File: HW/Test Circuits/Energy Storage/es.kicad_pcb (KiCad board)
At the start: 2 copper layers, 5 parts, among them J1 IN, J2 OUT

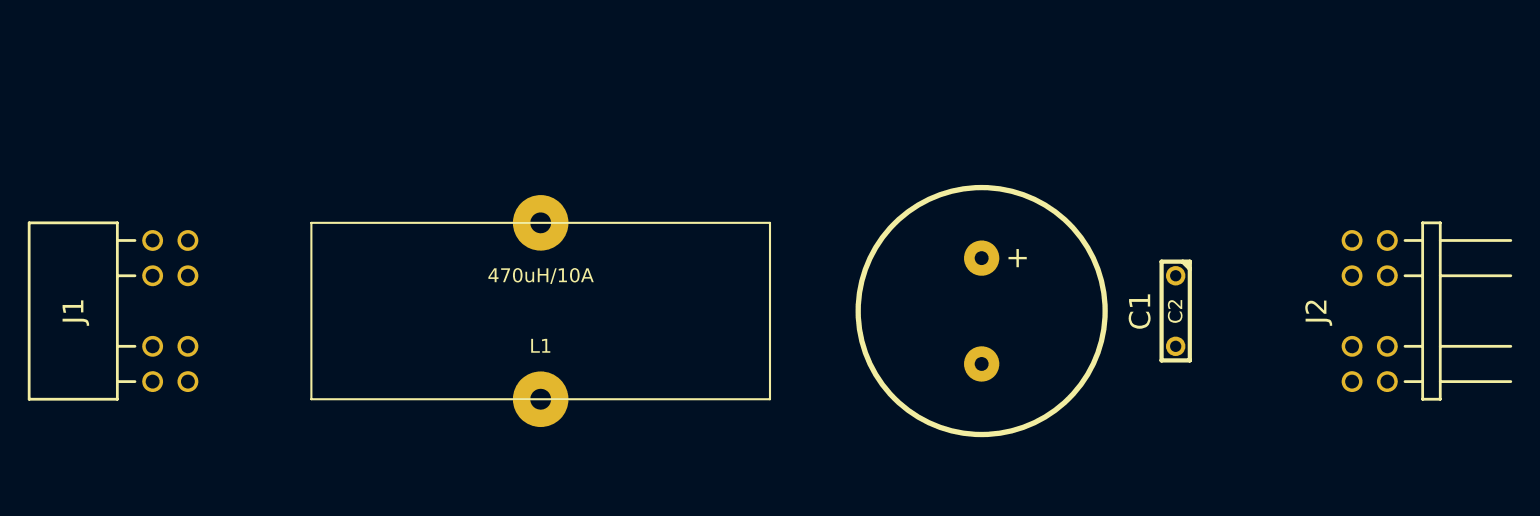
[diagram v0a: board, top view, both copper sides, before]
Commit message: Motor Measurement circuit added (not complete)
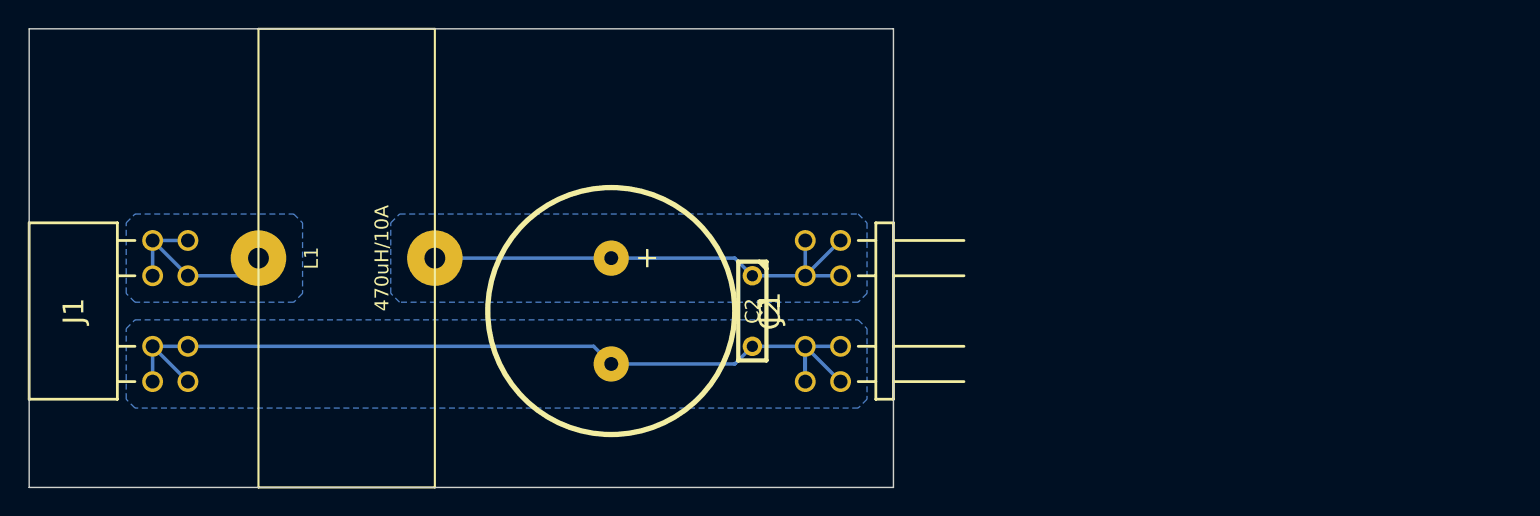
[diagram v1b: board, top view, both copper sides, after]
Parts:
- moved J2 39.4 mm to (121.9, 86.4)
- moved C2 30.5 mm to (116.8, 86.4)
- moved C1 26.7 mm to (106.7, 86.4)
- moved L1 14.5 mm to (87.6, 82.5), turned to 90 degrees
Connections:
- J1 pad 1: N-000001 -> GND
- J1 pad 10: GND -> N-000002
- J1 pad 2: N-000001 -> GND
- J1 pad 3: N-000001 -> GND
- J1 pad 4: N-000001 -> GND
- J1 pad 7: GND -> N-000002
- J1 pad 8: GND -> N-000002
- J1 pad 9: GND -> N-000002
- J2 pad 1: N-000003 -> GND
- J2 pad 10: GND -> N-000003
- J2 pad 2: N-000003 -> GND
- J2 pad 3: N-000003 -> GND
- J2 pad 4: N-000003 -> GND
- J2 pad 7: GND -> N-000003
- J2 pad 8: GND -> N-000003
- J2 pad 9: GND -> N-000003
- L1 pad 1: N-000001 -> N-000002
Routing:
- net GND: track 0.00 -> 65.4 mm
- net N-000003: track 0.00 -> 35.9 mm
- net N-000002: track 0.00 -> 14.3 mm
- added copper zone on B.Cu, net GND
- added copper zone on B.Cu, net N-000002
- added copper zone on B.Cu, net N-000003
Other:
- board outline added: 62.2 x 33 mm
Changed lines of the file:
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@@
   (general
     (links 19)
-    (no_connects 19)
-    (area 0 0 0 0)
+    (no_connects 0)
+    (area 64.415999 65.710999 134.454 99.389001)
     (thickness 1.6)
-    (drawings 0)
-    (tracks 0)
+    (drawings 4)
+    (tracks 24)
     (zones 0)
     (modules 5)
@@
     (user_trace_width 5)
     (trace_clearance 0.254)
-    (zone_clearance 0.508)
+    (zone_clearance 0.5)
     (zone_45_only no)
     (trace_min 0.254)
@@
   (net 0 "")
   (net 1 GND)
-  (net 2 N-000001)
+  (net 2 N-000002)
   (net 3 N-000003)
   (net_class Default "This is the default net class."
@@
     (add_net "")
     (add_net GND)
-    (add_net N-000001)
+    (add_net N-000002)
     (add_net N-000003)
   )
   (module MD-TEST-HDR-M (layer F.Cu)
-    (at 161.29 86.36 90)
+    (at 121.92 86.36 90)
     (fp_text reference J2 (at 0 -3.81 90) (layer F.SilkS)
       (effects (font (size 1.5 1.5) (thickness 0.2)))
@@
     (pad 1 thru_hole circle (at -5.08 1.27 90) (size 1.5 1.5) (drill 1)
       (layers *.Cu *.Mask F.SilkS)
-      (net 3 N-000003)
+      (net 1 GND)
     )
     (pad 2 thru_hole circle (at -5.08 -1.27 90) (size 1.5 1.5) (drill 1)
       (layers *.Cu *.Mask F.SilkS)
-      (net 3 N-000003)
+      (net 1 GND)
     )
     (pad 3 thru_hole circle (at -2.54 1.27 90) (size 1.5 1.5) (drill 1)
       (layers *.Cu *.Mask F.SilkS)
-      (net 3 N-000003)
+      (net 1 GND)
     )
     (pad 4 thru_hole circle (at -2.54 -1.27 90) (size 1.5 1.5) (drill 1)
       (layers *.Cu *.Mask F.SilkS)
-      (net 3 N-000003)
+      (net 1 GND)
     )
     (pad 7 thru_hole circle (at 2.54 1.27 90) (size 1.5 1.5) (drill 1)
       (layers *.Cu *.Mask F.SilkS)
-      (net 1 GND)
+      (net 3 N-000003)
     )
     (pad 9 thru_hole circle (at 5.08 1.27 90) (size 1.5 1.5) (drill 1)
       (layers *.Cu *.Mask F.SilkS)
-      (net 1 GND)
+      (net 3 N-000003)
     )
     (pad 10 thru_hole circle (at 5.08 -1.27 90) (size 1.5 1.5) (drill 1)
       (layers *.Cu *.Mask F.SilkS)
-      (net 1 GND)
+      (net 3 N-000003)
     )
     (pad 8 thru_hole circle (at 2.54 -1.27 90) (size 1.5 1.5) (drill 1)
       (layers *.Cu *.Mask F.SilkS)
-      (net 1 GND)
+      (net 3 N-000003)
     )
   )
@@
     (pad 1 thru_hole circle (at -5.08 -1.27 90) (size 1.5 1.5) (drill 1)
       (layers *.Cu *.Mask F.SilkS)
-      (net 2 N-000001)
+      (net 1 GND)
     )
     (pad 2 thru_hole circle (at -5.08 1.27 90) (size 1.5 1.5) (drill 1)
       (layers *.Cu *.Mask F.SilkS)
-      (net 2 N-000001)
+      (net 1 GND)
     )
     (pad 3 thru_hole circle (at -2.54 -1.27 90) (size 1.5 1.5) (drill 1)
       (layers *.Cu *.Mask F.SilkS)
-      (net 2 N-000001)
+      (net 1 GND)
     )
     (pad 4 thru_hole circle (at -2.54 1.27 90) (size 1.5 1.5) (drill 1)
       (layers *.Cu *.Mask F.SilkS)
-      (net 2 N-000001)
+      (net 1 GND)
     )
     (pad 7 thru_hole circle (at 2.54 -1.27 90) (size 1.5 1.5) (drill 1)
       (layers *.Cu *.Mask F.SilkS)
-      (net 1 GND)
+      (net 2 N-000002)
     )
     (pad 8 thru_hole circle (at 2.54 1.27 90) (size 1.5 1.5) (drill 1)
       (layers *.Cu *.Mask F.SilkS)
-      (net 1 GND)
+      (net 2 N-000002)
     )
     (pad 9 thru_hole circle (at 5.08 -1.27 90) (size 1.5 1.5) (drill 1)
       (layers *.Cu *.Mask F.SilkS)
-      (net 1 GND)
+      (net 2 N-000002)
     )
     (pad 10 thru_hole circle (at 5.08 1.27 90) (size 1.5 1.5) (drill 1)
       (layers *.Cu *.Mask F.SilkS)
-      (net 1 GND)
+      (net 2 N-000002)
     )
   )
   (module L-TOROID-D35X5 (layer F.Cu)
-    (at 101.6 86.36 180)
-    (fp_text reference L1 (at 0 -2.54 180) (layer F.SilkS)
+    (at 87.63 82.55 90)
+    (fp_text reference L1 (at 0 -2.54 90) (layer F.SilkS)
       (effects (font (size 1 1) (thickness 0.15)))
     )
-    (fp_text value 470uH/10A (at 0 2.54 180) (layer F.SilkS)
+    (fp_text value 470uH/10A (at 0 2.54 90) (layer F.SilkS)
       (effects (font (size 1 1) (thickness 0.15)))
     )
@@
     (fp_line (start 16.51 6.35) (end -16.51 6.35) (layer F.SilkS) (width 0.15))
     (fp_line (start -16.51 6.35) (end -16.51 -6.35) (layer F.SilkS) (width 0.15))
-    (pad 1 thru_hole circle (at 0 -6.35 180) (size 4 4) (drill 1.5)
-      (layers *.Cu *.Mask F.SilkS)
-      (net 2 N-000001)
-    )
-    (pad 2 thru_hole circle (at 0 6.35 180) (size 4 4) (drill 1.5)
+    (pad 1 thru_hole circle (at 0 -6.35 90) (size 4 4) (drill 1.5)
+      (layers *.Cu *.Mask F.SilkS)
+      (net 2 N-000002)
+    )
+    (pad 2 thru_hole circle (at 0 6.35 90) (size 4 4) (drill 1.5)
       (layers *.Cu *.Mask F.SilkS)
       (net 3 N-000003)
@@
   )
   (module C3P_D7 (layer F.Cu)
-    (at 133.35 86.36 270)
+    (at 106.68 86.36 270)
     (fp_text reference C1 (at 0 -11.43 270) (layer F.SilkS)
       (effects (font (size 1.524 1.524) (thickness 0.3048)))
@@
   )
   (module C2 (layer F.Cu)
-    (at 147.32 86.36 270)
+    (at 116.84 86.36 270)
     (descr "Condensateur = 2 pas")
     (tags C)
@@
     )
   )
+  (gr_line (start 64.77 99.06) (end 64.77 66.04) (angle 90) (layer Edge.Cuts) (width 0.1))
+  (gr_line (start 127 99.06) (end 64.77 99.06) (angle 90) (layer Edge.Cuts) (width 0.1))
+  (gr_line (start 127 66.04) (end 127 99.06) (angle 90) (layer Edge.Cuts) (width 0.1))
+  (gr_line (start 64.77 66.04) (end 127 66.04) (angle 90) (layer Edge.Cuts) (width 0.1))
+  (segment (start 120.65 88.9) (end 123.19 91.44) (width 0.254) (layer B.Cu) (net 1))
+  (segment (start 116.84 88.9) (end 120.65 88.9) (width 0.254) (layer B.Cu) (net 1))
+  (segment (start 120.65 88.9) (end 120.65 91.44) (width 0.254) (layer B.Cu) (net 1))
+  (segment (start 120.65 91.44) (end 120.65 88.9) (width 0.254) (layer B.Cu) (net 1))
+  (segment (start 120.65 88.9) (end 123.19 88.9) (width 0.254) (layer B.Cu) (net 1))
+  (segment (start 106.68 90.17) (end 115.57 90.17) (width 0.254) (layer B.Cu) (net 1))
+  (segment (start 115.57 90.17) (end 116.84 88.9) (width 0.254) (layer B.Cu) (net 1))
+  (segment (start 76.2 88.9) (end 105.41 88.9) (width 0.254) (layer B.Cu) (net 1))
+  (segment (start 105.41 88.9) (end 106.68 90.17) (width 0.254) (layer B.Cu) (net 1))
+  (segment (start 73.66 88.9) (end 76.2 91.44) (width 0.254) (layer B.Cu) (net 1))
+  (segment (start 73.66 88.9) (end 73.66 91.44) (width 0.254) (layer B.Cu) (net 1))
+  (segment (start 73.66 88.9) (end 76.2 88.9) (width 0.254) (layer B.Cu) (net 1))
+  (segment (start 76.2 83.82) (end 80.01 83.82) (width 0.254) (layer B.Cu) (net 2))
+  (segment (start 80.01 83.82) (end 81.28 82.55) (width 0.254) (layer B.Cu) (net 2))
+  (segment (start 73.66 81.28) (end 73.66 83.82) (width 0.254) (layer B.Cu) (net 2))
+  (segment (start 76.2 81.28) (end 73.66 81.28) (width 0.254) (layer B.Cu) (net 2))
+  (segment (start 73.66 81.28) (end 76.2 83.82) (width 0.254) (layer B.Cu) (net 2))
+  (segment (start 106.68 82.55) (end 115.57 82.55) (width 0.254) (layer B.Cu) (net 3))
+  (segment (start 115.57 82.55) (end 116.84 83.82) (width 0.254) (layer B.Cu) (net 3))
+  (segment (start 93.98 82.55) (end 106.68 82.55) (width 0.254) (layer B.Cu) (net 3))
+  (segment (start 120.65 83.82) (end 123.19 81.28) (width 0.254) (layer B.Cu) (net 3))
+  (segment (start 120.65 83.82) (end 123.19 83.82) (width 0.254) (layer B.Cu) (net 3))
+  (segment (start 120.65 83.82) (end 120.65 81.28) (width 0.254) (layer B.Cu) (net 3))
+  (segment (start 116.84 83.82) (end 120.65 83.82) (width 0.254) (layer B.Cu) (net 3))
+  (zone (net 2) (net_name N-000002) (layer B.Cu) (hatch edge 0.508)
+    (connect_pads yes (clearance 0.5))
+    (min_thickness 0.254)
+    (fill (arc_segments 16) (thermal_gap 0.508) (thermal_bridge_width 0.508))
+    (polygon
+      (pts
+        (xy 84.455 85.09) (xy 83.82 85.725) (xy 72.39 85.725) (xy 71.755 85.09) (xy 71.755 80.01)
+        (xy 72.39 79.375) (xy 83.82 79.375) (xy 84.455 80.01)
+      )
+    )
+  )
+  (zone (net 3) (net_name N-000003) (layer B.Cu) (hatch edge 0.508)
+    (connect_pads yes (clearance 0.5))
+    (min_thickness 0.254)
+    (fill (arc_segments 16) (thermal_gap 0.508) (thermal_bridge_width 0.508))
+    (polygon
+      (pts
+        (xy 125.095 85.09) (xy 124.46 85.725) (xy 91.44 85.725) (xy 90.805 85.09) (xy 90.805 80.01)
+        (xy 91.44 79.375) (xy 124.46 79.375) (xy 125.095 80.01)
+      )
+    )
+  )
+  (zone (net 1) (net_name GND) (layer B.Cu) (hatch edge 0.508)
+    (connect_pads yes (clearance 0.5))
+    (min_thickness 0.254)
+    (fill (arc_segments 16) (thermal_gap 0.508) (thermal_bridge_width 0.508))
+    (polygon
+      (pts
+        (xy 125.095 92.71) (xy 124.46 93.345) (xy 72.39 93.345) (xy 71.755 92.71) (xy 71.755 87.63)
+        (xy 72.39 86.995) (xy 124.46 86.995) (xy 125.095 87.63)
+      )
+    )
+  )
